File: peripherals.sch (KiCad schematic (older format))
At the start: 0 parts

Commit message: Add scheme for SIM card
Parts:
- added C?: C_100n_0402, antmicro-footprints:0402-cap, symbol antmicroCapacitors0402:C_100n_0402
- added C? (x3): C_22p_0402, antmicro-footprints:0402-cap, symbol antmicroCapacitors0402:C_22p_0402
- added D2: PUSB3F96X_PASS, antmicro-footprints:PUSB3F96X, symbol antmicroTVSDiodes:PUSB3F96X_PASS
- added J1: 693022010811, antmicro-footprints:693022010811, symbol antmicroSimCardConnectors:693022010811
- added R? (x3): R_22R_0402, antmicro-footprints:0402-res, symbol antmicroResistors0402:R_22R_0402
- added R?: R_10k_0402, antmicro-footprints:0402-res, symbol antmicroResistors0402:R_10k_0402
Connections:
- new net: C?.1, D2.2 (CH2), D2.9 (CH2), J1.C2 (RST), R?.2
- new net: C?.1, D2.4 (CH3), D2.7 (CH3), J1.C3 (CLK), R?.2
- new net: C?.1, D2.5 (CH4), D2.6 (CH4), J1.C7 (I/O), R?.2, R?.2
- new net GND: C?.2, C?.2, C?.2, C?.2, D2.3 (GND), D2.8 (GND), J1.C5 (GND), J1.Z1 (GND), J1.Z2 (GND)
- new net USIM1_CLK: R?.1
- new net USIM1_DATA: R?.1
- new net USIM1_RST: R?.1
- new net USIM1_VDD: C?.1, D2.1 (CH1), D2.10 (CH1), J1.C1 (VCC), R?.1
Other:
- note added: "Main micro SIM connector"

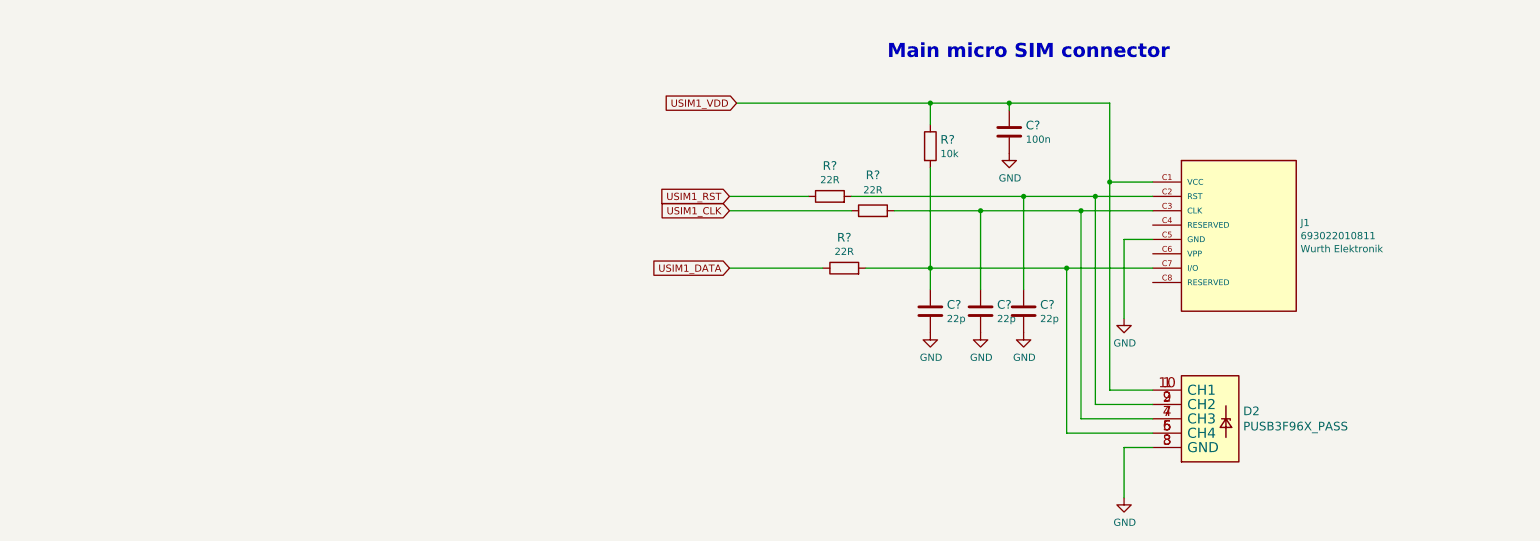
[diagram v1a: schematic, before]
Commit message: Creating schema for SD card connection
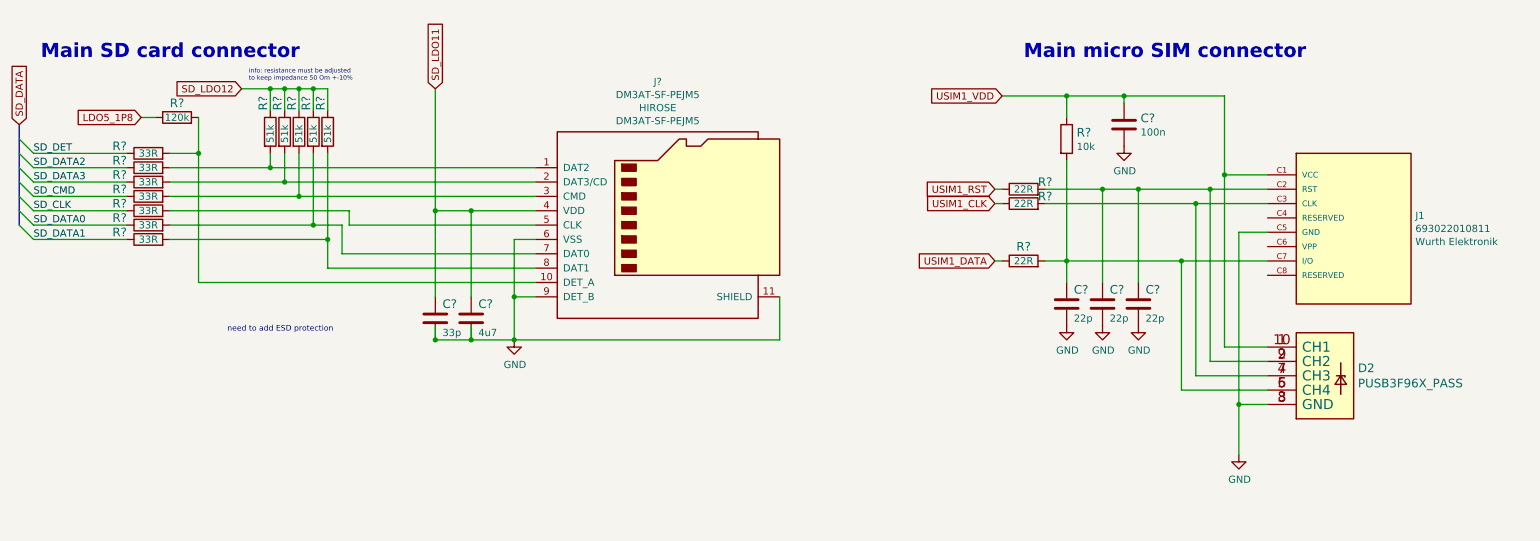
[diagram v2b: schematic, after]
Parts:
- added C?: C_4u7_0402, antmicro-footprints:0402-cap, symbol antmicroCapacitors0402:C_4u7_0402
- added C?: C_33p_0402, antmicro-footprints:0402-cap, symbol antmicroCapacitors0402:C_33p_0402
- added J?: DM3AT-SF-PEJM5, antmicro-footprints:MicroSD_DM3AT-SF-PEJM5, symbol antmicroMemoryConnectorsPCCardSockets:DM3AT-SF-PEJM5
- added R? (x7): R_33R_0402, antmicro-footprints:0402-res, symbol antmicroResistors0402:R_33R_0402
- added R? (x5): R_51k_0603, antmicro-footprints:0603-res, symbol antmicroResistors0603:R_51k_0603
- added R?: R_120k_0402, antmicro-footprints:0402-res, symbol antmicroResistors0402:R_120k_0402
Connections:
- net GND: now also C?.2, C?.2, J?.11 (SHIELD), J?.6 (VSS), J?.9 (DET_B)
- net at C?.1, D2.2 (CH2), D2.9 (CH2)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: now also C?.1
- net at D2.4 (CH3), D2.7 (CH3), J1.C3 (CLK)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: no longer C?.1
- new net: J?.10 (DET_A), R?.2, R?.2
- new net: J?.8 (DAT1), R?.2, R?.2
- new net: J?.2 (DAT3/CD), R?.2, R?.2
- new net: J?.1 (DAT2), R?.2, R?.2
- new net: J?.3 (CMD), R?.2, R?.2
- new net: J?.5 (CLK), R?.2
- new net: J?.7 (DAT0), R?.2, R?.2
- new net LDO5_1P8: R?.1
- new net SD_CLK: R?.1
- new net SD_CMD: R?.1
- new net SD_DATA0: R?.1
- new net SD_DATA1: R?.1
- new net SD_DATA2: R?.1
- new net SD_DATA3: R?.1
- new net SD_DET: R?.1
- new net SD_LDO11: C?.1, C?.1, J?.4 (VDD)
- new net SD_LDO12: R?.1, R?.1, R?.1, R?.1, R?.1
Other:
- note added: "Main SD card connector"
- note added: "info: resistance must be adjusted \nto keep impedance 50 Om +-10%"
- note added: "need to add ESD protection\n"
- moved on the sheet: C?, D2, J1, R?

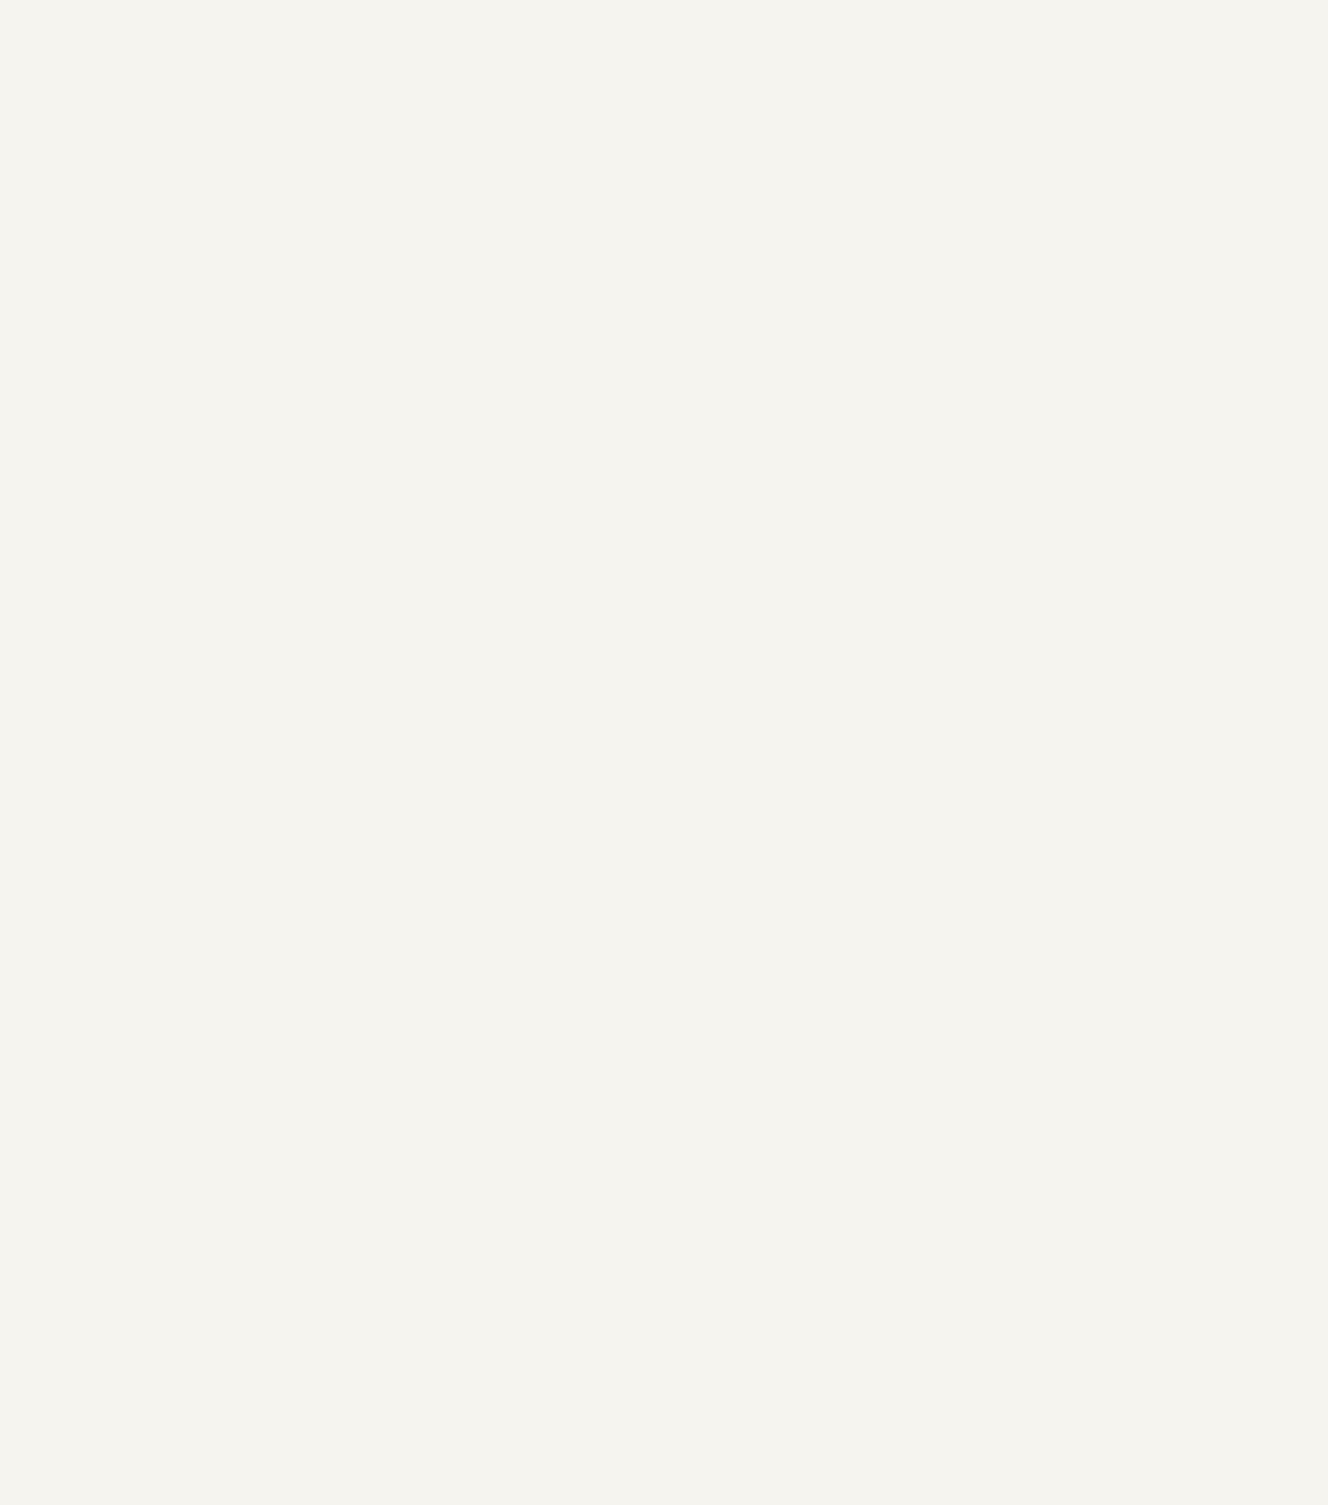
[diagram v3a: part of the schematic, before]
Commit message: Added schema of Main and GNSS Antenna
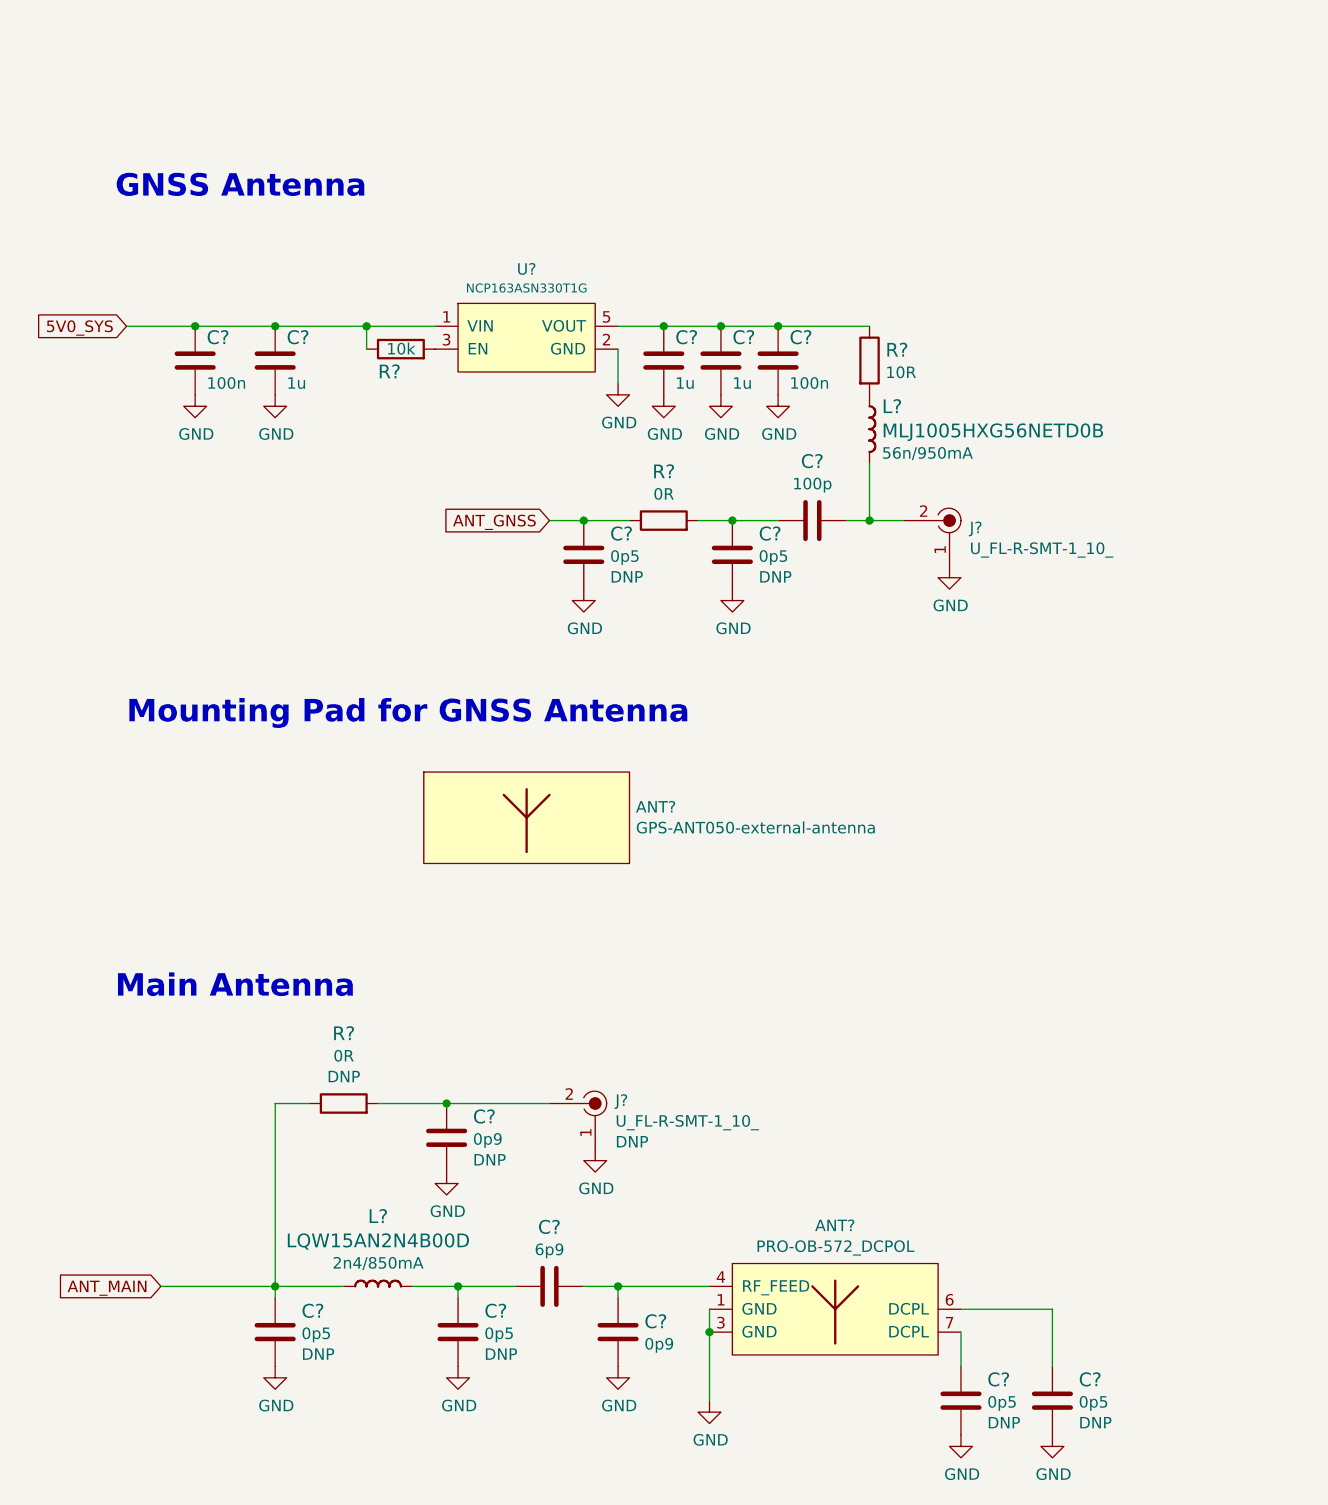
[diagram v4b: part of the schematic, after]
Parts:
- added ANT?: GPS-ANT050-external-antenna, antmicro-footprints:GPS-ANT050-mounting-pad, symbol antmicroRFAntennas:GPS-ANT050-external-antenna
- added ANT?: PRO-OB-572_DCPOL, antmicro-footprints:PRO-OB-572_2, symbol antmicroRFAntennas:PRO-OB-572_DCPOL
- added C? (x2): C_100n_0402, antmicro-footprints:0402-cap, symbol antmicroCapacitors0402:C_100n_0402
- added C? (x3): C_1u_0402, antmicro-footprints:0402-cap, symbol antmicroCapacitors0402:C_1u_0402
- added C?: C_100p_0402, antmicro-footprints:0402-cap, symbol antmicroCapacitors0402:C_100p_0402
- added C? (x6): C_0p5_0402, antmicro-footprints:0402-cap, symbol antmicroCapacitors0402:C_0p5_0402
- added C? (x2): C_0p9_0402, antmicro-footprints:0402-cap, symbol antmicroCapacitors0402:C_0p9_0402
- added C?: C_6p9_0402, antmicro-footprints:0402-cap, symbol antmicroCapacitors0402:C_6p9_0402
- added J? (x2): U_FL-R-SMT-1_10_, antmicro-footprints:Coax_Conn_U.FL, symbol antmicroCoaxialConnectorsRF:U_FL-R-SMT-1_10_
- added L?: MLJ1005HXG56NETD0B, antmicro-footprints:0402-res, symbol antmicroFixedInductors:MLJ1005HXG56NETD0B
- added L?: LQW15AN2N4B00D, antmicro-footprints:0402-res, symbol antmicroFixedInductors:LQW15AN2N4B00D
- added R?: R_10k_0402, antmicro-footprints:0402-res, symbol antmicroResistors0402:R_10k_0402
- added R?: R_10R_0603, antmicro-footprints:0603-res, symbol antmicroResistors0603:R_10R_0603
- added R? (x2): R_0R_0402, antmicro-footprints:0402-res, symbol antmicroResistors0402:R_0R_0402
- added U?: NCP163ASN330T1G, antmicro-footprints:SOT-23-5, symbol antmicroPMICVoltageRegulatorsLinear:NCP163ASN330T1G
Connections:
- net GND: now also ANT?.1 (GND), ANT?.3 (GND), C?.2, C?.2, C?.2, C?.2, C?.2, C?.2, C?.2, C?.2, C?.2, C?.2, C?.2, C?.2, C?.2, J?.1, J?.1, U?.2 (GND)
- new net: C?.1, J?.2, L?.2 (P)
- new net: R?.2, U?.3 (EN)
- new net: C?.1, C?.1, C?.1, R?.1, U?.5 (VOUT)
- new net: L?.1 (P), R?.2
- new net: C?.1, C?.2, R?.2
- new net: C?.1, J?.2, R?.2
- new net: C?.1, C?.2, L?.2 (P)
- new net: ANT?.4 (RF_FEED), C?.1, C?.1
- new net: ANT?.7 (DCPL), C?.1
- new net: ANT?.6 (DCPL), C?.1
- new net 5V0_SYS: C?.1, C?.1, R?.1, U?.1 (VIN)
- new net ANT_GNSS: C?.1, R?.1
- new net ANT_MAIN: C?.1, L?.1 (P), R?.1
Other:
- note added: "GNSS Antenna\n"
- note added: "Main Antenna\n"
- note added: "Mounting Pad for GNSS Antenna\n"

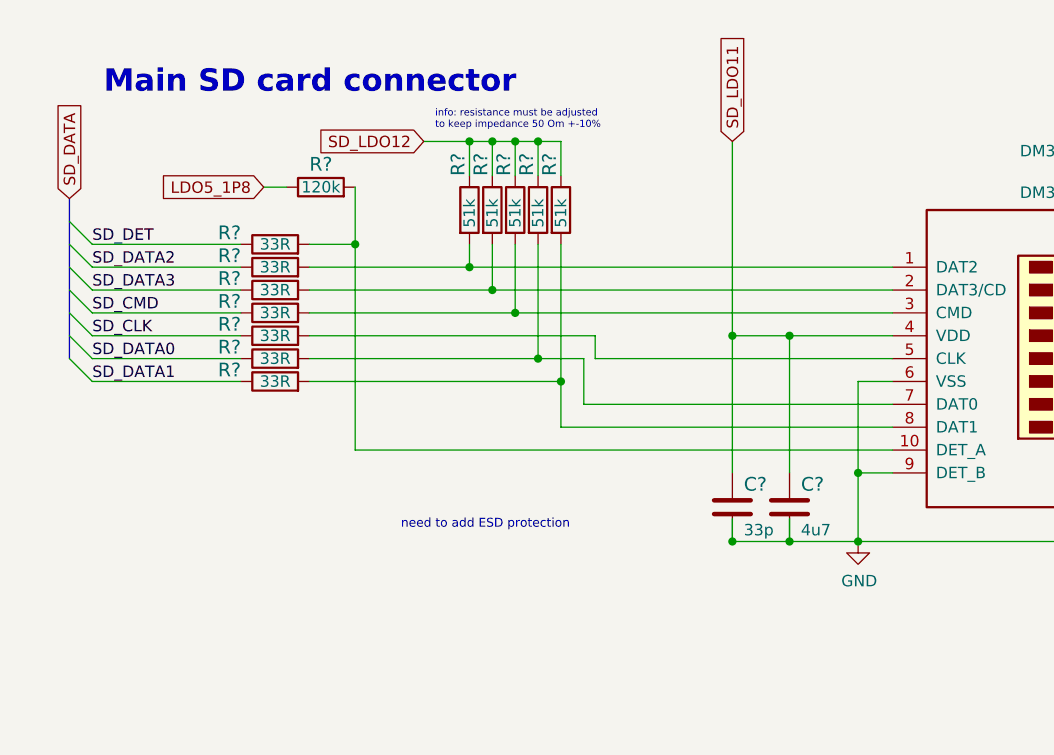
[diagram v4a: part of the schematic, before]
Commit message: Added ESD protection to SD card
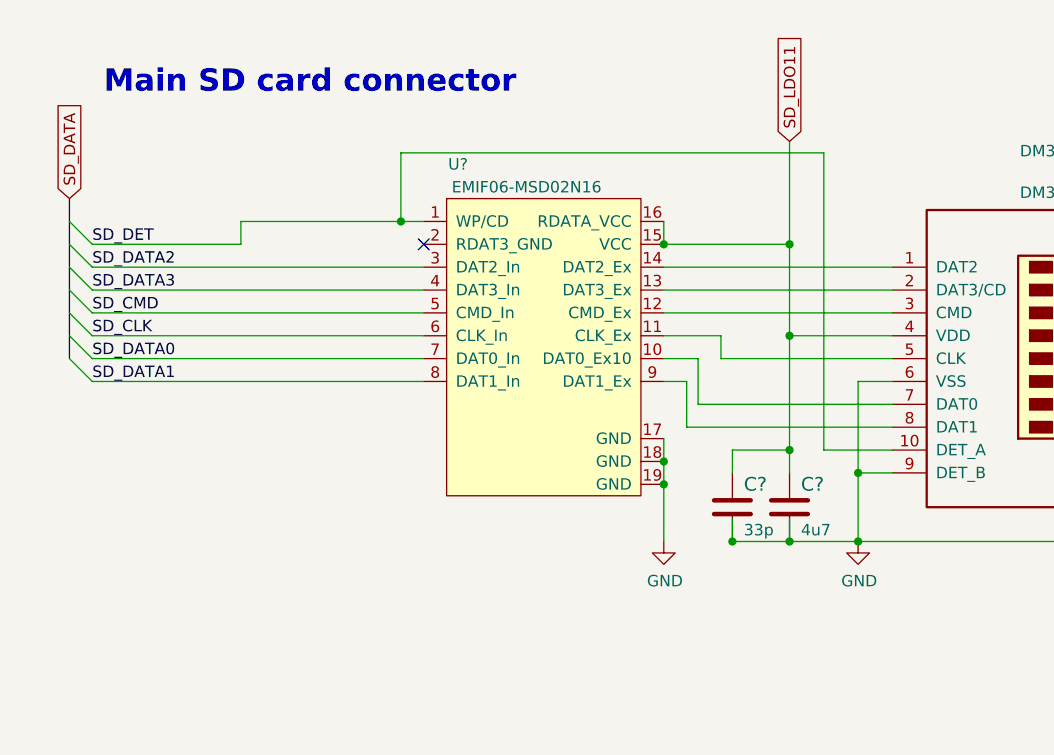
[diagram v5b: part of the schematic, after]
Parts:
- removed R? (x7): R_33R_0402, antmicro-footprints:0402-res, symbol antmicroResistors0402:R_33R_0402
- removed R? (x5): R_51k_0603, antmicro-footprints:0603-res, symbol antmicroResistors0603:R_51k_0603
- removed R?: R_120k_0402, antmicro-footprints:0402-res, symbol antmicroResistors0402:R_120k_0402
- added U?: EMIF06-MSD02N16, symbol antmicroPowerProtection:EMIF06-MSD02N16
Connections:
- net GND: now also U?.17 (GND), U?.18 (GND), U?.19 (GND)
- net SD_CLK: now also U?.6 (CLK_In)
- net SD_CMD: now also U?.5 (CMD_In)
- net SD_DATA0: now also U?.7 (DAT0_In)
- net SD_DATA1: now also U?.8 (DAT1_In)
- net SD_DATA2: now also U?.3 (DAT2_In)
- net SD_DATA3: now also U?.4 (DAT3_In)
- net SD_DET: now also J?.10 (DET_A), U?.1 (WP/CD)
- net SD_LDO11: now also U?.15 (VCC), U?.16 (RDATA_VCC)
- net at J?.8 (DAT1): now also U?.9 (DAT1_Ex)
- net at J?.2 (DAT3/CD): now also U?.13 (DAT3_Ex)
- net at J?.1 (DAT2): now also U?.14 (DAT2_Ex)
- net at J?.3 (CMD): now also U?.12 (CMD_Ex)
- net at J?.5 (CLK): now also U?.11 (CLK_Ex)
- net at J?.7 (DAT0): now also U?.10 (DAT0_Ex10)
- no-connect marks 0 -> 1
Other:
- note removed: "info: resistance must be adjusted \nto keep impedance 50 Om +-10%"
- note removed: "need to add ESD protection\n"
